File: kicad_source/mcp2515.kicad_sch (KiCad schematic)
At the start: 15 parts, among them CN4 SM04B-GHS-TB, CN5 SM04B-GHS-TB, U8 MCP2515T-I/SO, U9 SN65HVD230, Y1 X322516MLB4SI

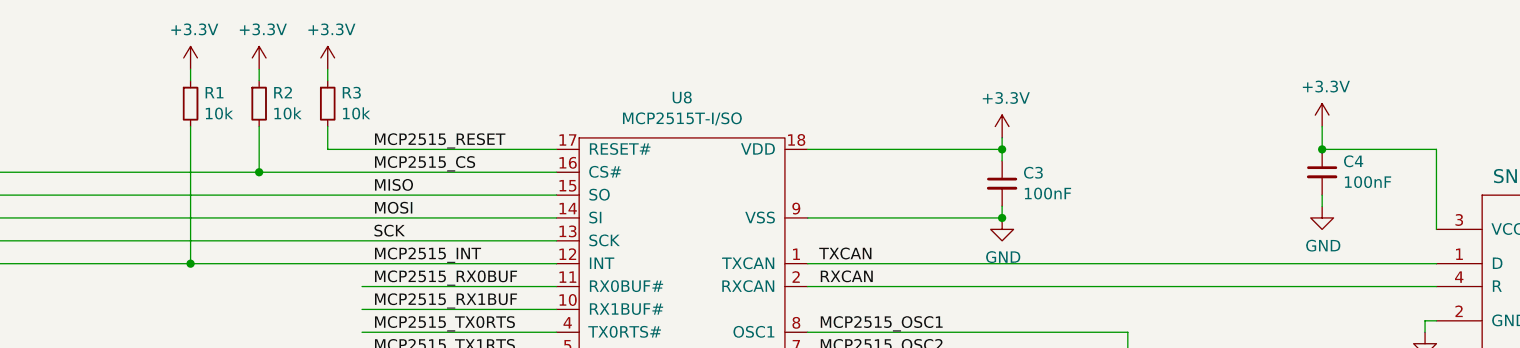
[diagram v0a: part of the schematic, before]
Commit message: removed unnecessary parts
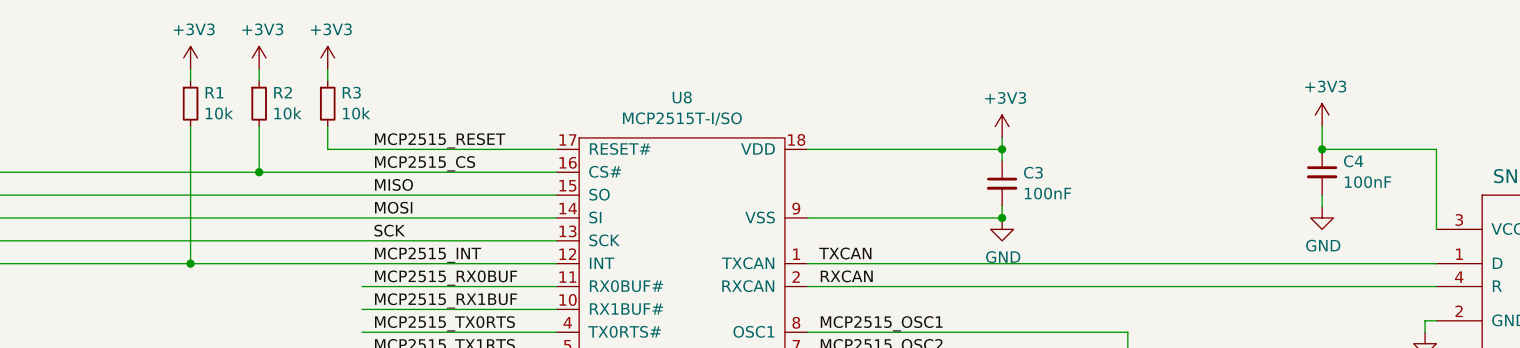
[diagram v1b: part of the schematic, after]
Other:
- title: OpenCyphalPicoBase -> CyphalGNSSIMUBase/CAN
